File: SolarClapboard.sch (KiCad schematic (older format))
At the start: 52 parts, among them J1 TEST_1P, J2 TEST_1P, U1 MCP73871, U2 MPL3115A2, U3 HIH6130-I2C, U4 LT3011, U5 Teensy3.2

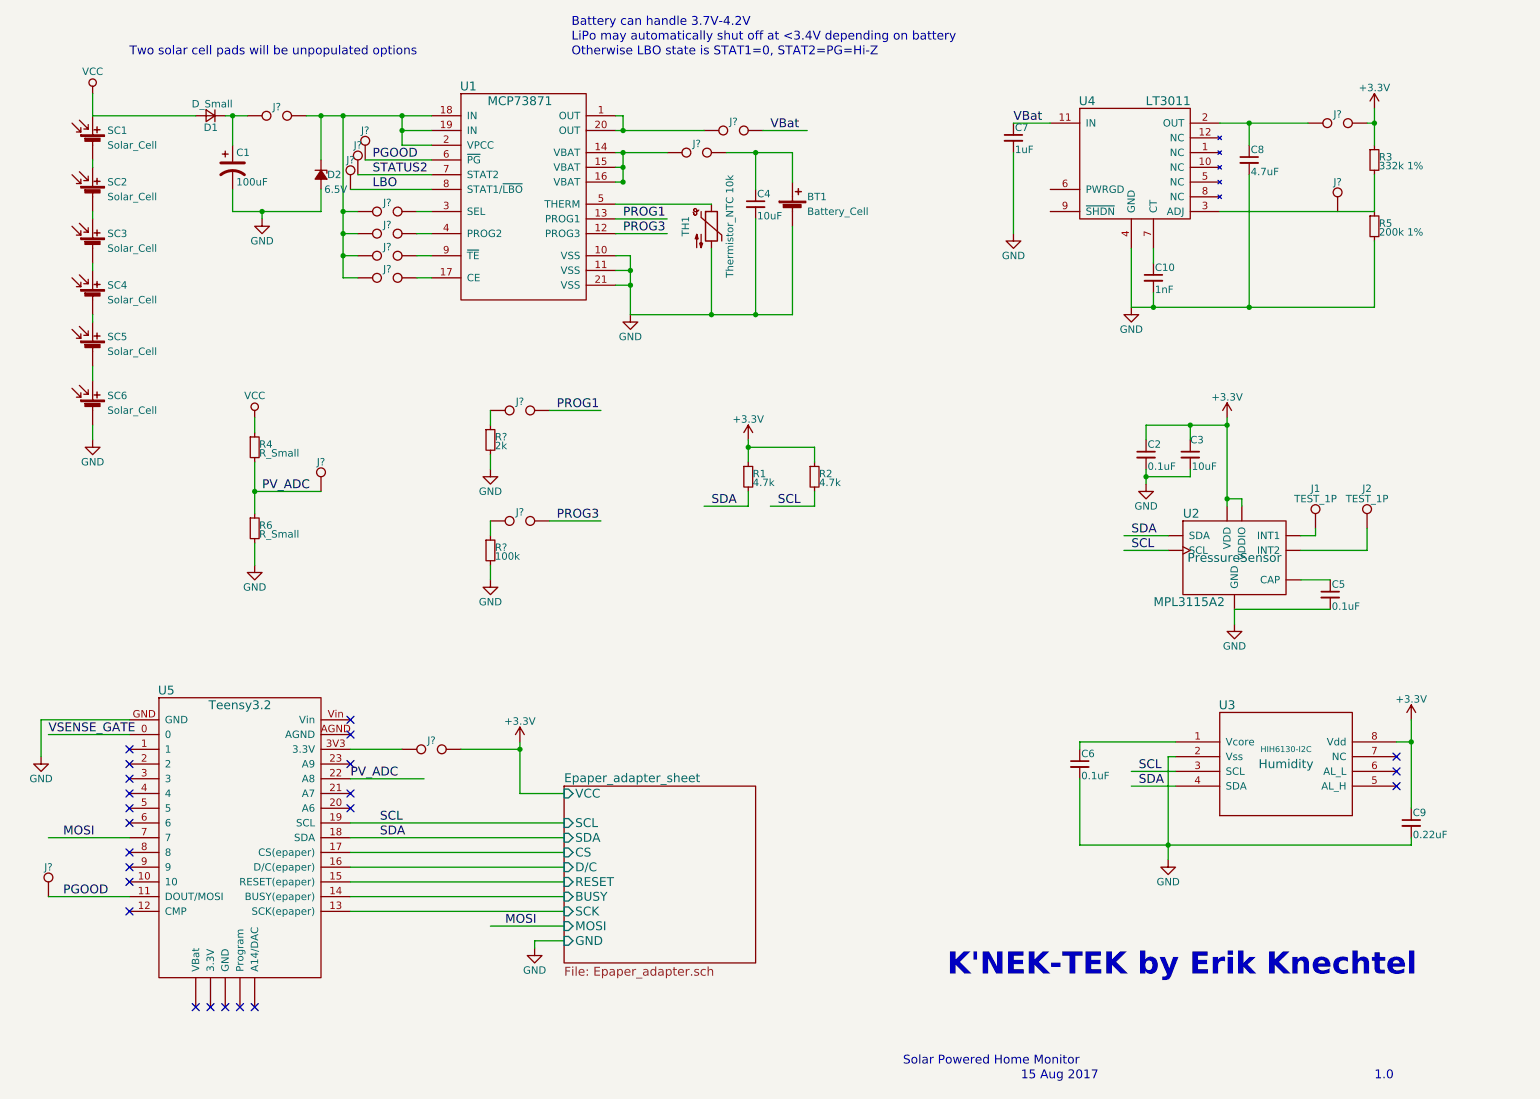
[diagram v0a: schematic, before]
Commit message: Add files via upload
Trying to figure out whether to hook up the PGOOD and PWRGOOD and SHDN and so on.
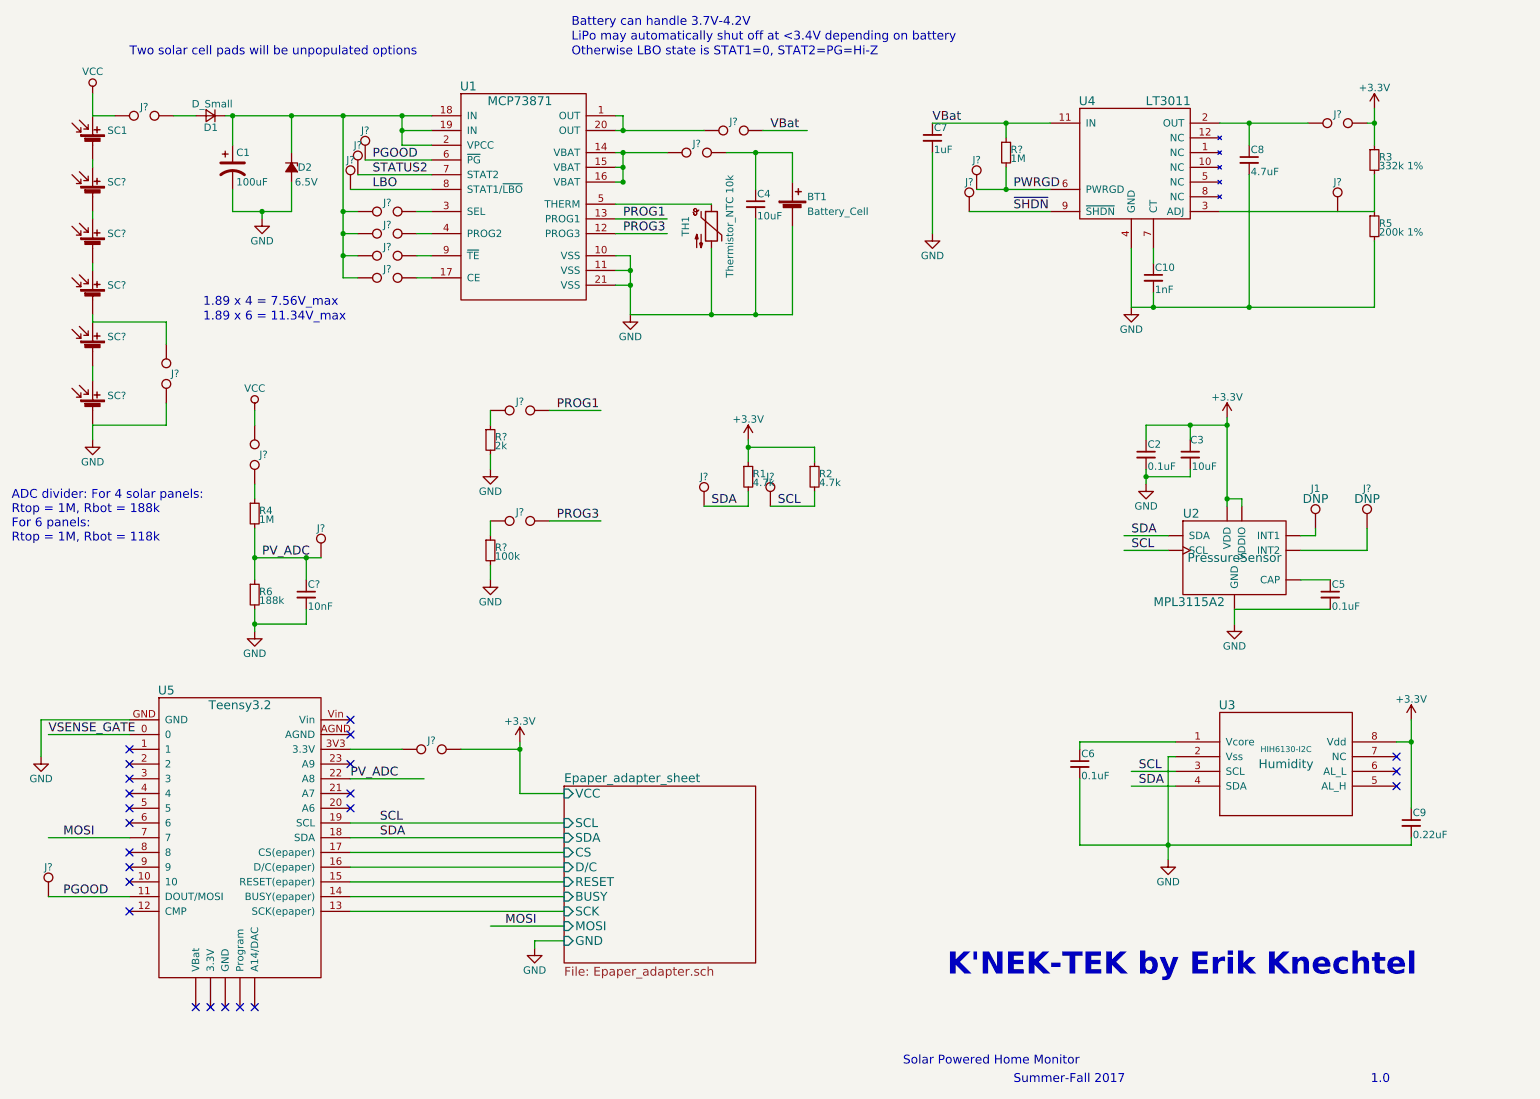
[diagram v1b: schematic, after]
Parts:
- removed J2: TEST_1P, symbol TEST_1P
- removed SC2, SC3, SC4, SC5, SC6: Solar_Cell, symbol Solar_Cell
- added C?: 10nF, symbol C_Small
- added J? (x2): TEST_2P, symbol TEST_2P
- added J? (x5): TEST_1P, symbol TEST_1P
- added R?: 1M, symbol R_Small
- added SC? (x5): Solar_Cell, symbol Solar_Cell
- J1: DNP (none) -> DNP
- R4: value R_Small -> 1M
- R6: value R_Small -> 188k
- SC1: MFG_PN (none) -> KXOB22-04X3F; Max_Current (none) -> 15mA; Max_Voltage (none) -> 1.89V; PMPP Current 18mA -> (none); PMPP Voltage 6.06V -> (none)
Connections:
- net labels added: PWRGD, ~SHDN
- wire segments 133 -> 145
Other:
- note added: "1.89 x 4 = 7.56V_max"
- note added: "1.89 x 6 = 11.34V_max"
- note added: "ADC divider: For 4 solar panels:\nRtop = 1M, Rbot = 188k\nFor 6 panels:\nRtop = 1M, Rbot = 118k\n"
- note added: "Summer-Fall 2017"
- note removed: "15 Aug 2017"
- moved on the sheet: C7, D2, J?, R4, R6

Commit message: Add files via upload
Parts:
- BT1: footprint (none) -> Connectors_JST:JST_PH_S2B-PH-SM4-TB_02x2.00mm_Angled
- J23: renamed from J?; footprint (none) -> Wire_Pads:SolderWirePad_single_1-2mmDrill
- U4: renamed from U3; footprint MODULE -> (none)
- gave numbers to parts that had none: 32
- renumbered C7 to C1, C6 to C10, C9 to C11, C8 to C2, C1 to C3, C10 to C5, C2 to C6, C3 to C7, C5 to C9, J1 to J21, R3 to R2, R5 to R3, R1 to R5, R2 to R6, R4 to R7, R6 to R9, U4 to U2, U2 to U3
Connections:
- net labels removed: VSENSE_GATE
- no-connect marks 23 -> 24
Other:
- moved on the sheet: J11

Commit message: Add files via upload
Working on the BOM and footprints.
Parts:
- C1, C10, C11, C2, C5, C6, C8, C9: footprint (none) -> Capacitors_SMD:C_1206_HandSoldering
- C3, C4: footprint (none) -> Capacitors_THT:CP_Radial_D5.0mm_P2.00mm
- J1, J12, J13, J14, J15, J16, J17, J2, J20, J24, J3, J4, J9: footprint (none) -> Measurement_Points:Test_Point_2Pads
- TP1: renamed from J7; footprint (none) -> Wire_Pads:SolderWirePad_single_1-2mmDrill
- TP10: renamed from J22; footprint (none) -> Wire_Pads:SolderWirePad_single_1-2mmDrill
- TP2: renamed from J6; footprint (none) -> Wire_Pads:SolderWirePad_single_1-2mmDrill
- TP3: renamed from J5; footprint (none) -> Wire_Pads:SolderWirePad_single_1-2mmDrill
- TP4: renamed from J25; footprint (none) -> Wire_Pads:SolderWirePad_single_1-2mmDrill
- TP6: renamed from J18; footprint (none) -> Wire_Pads:SolderWirePad_single_1-2mmDrill
- TP7: renamed from J19; footprint (none) -> Wire_Pads:SolderWirePad_single_1-2mmDrill
- TP8: renamed from J21; footprint (none) -> Wire_Pads:SolderWirePad_single_1-2mmDrill
- TP9: renamed from J11; footprint (none) -> Wire_Pads:SolderWirePad_single_1-2mmDrill
- U1: footprint (none) -> Housings_DFN_QFN:QFN-20-1EP_4x4mm_Pitch0.5mm; symbol MCP73871 -> MCP73871-RESCUE-SolarClapboard
- U2: footprint (none) -> Housings_SSOP:MSOP-12_3x4mm_Pitch0.65mm
- U3: footprint (none) -> CustomFootprints:LGA-8_3x5mm_Pitch1.25mm_handsolder
- U4: footprint (none) -> Housings_SOIC:SO-8_5.3x6.2mm_Pitch1.27mm
- renumbered J10 to TP30, J8 to TP31, J23 to TP5

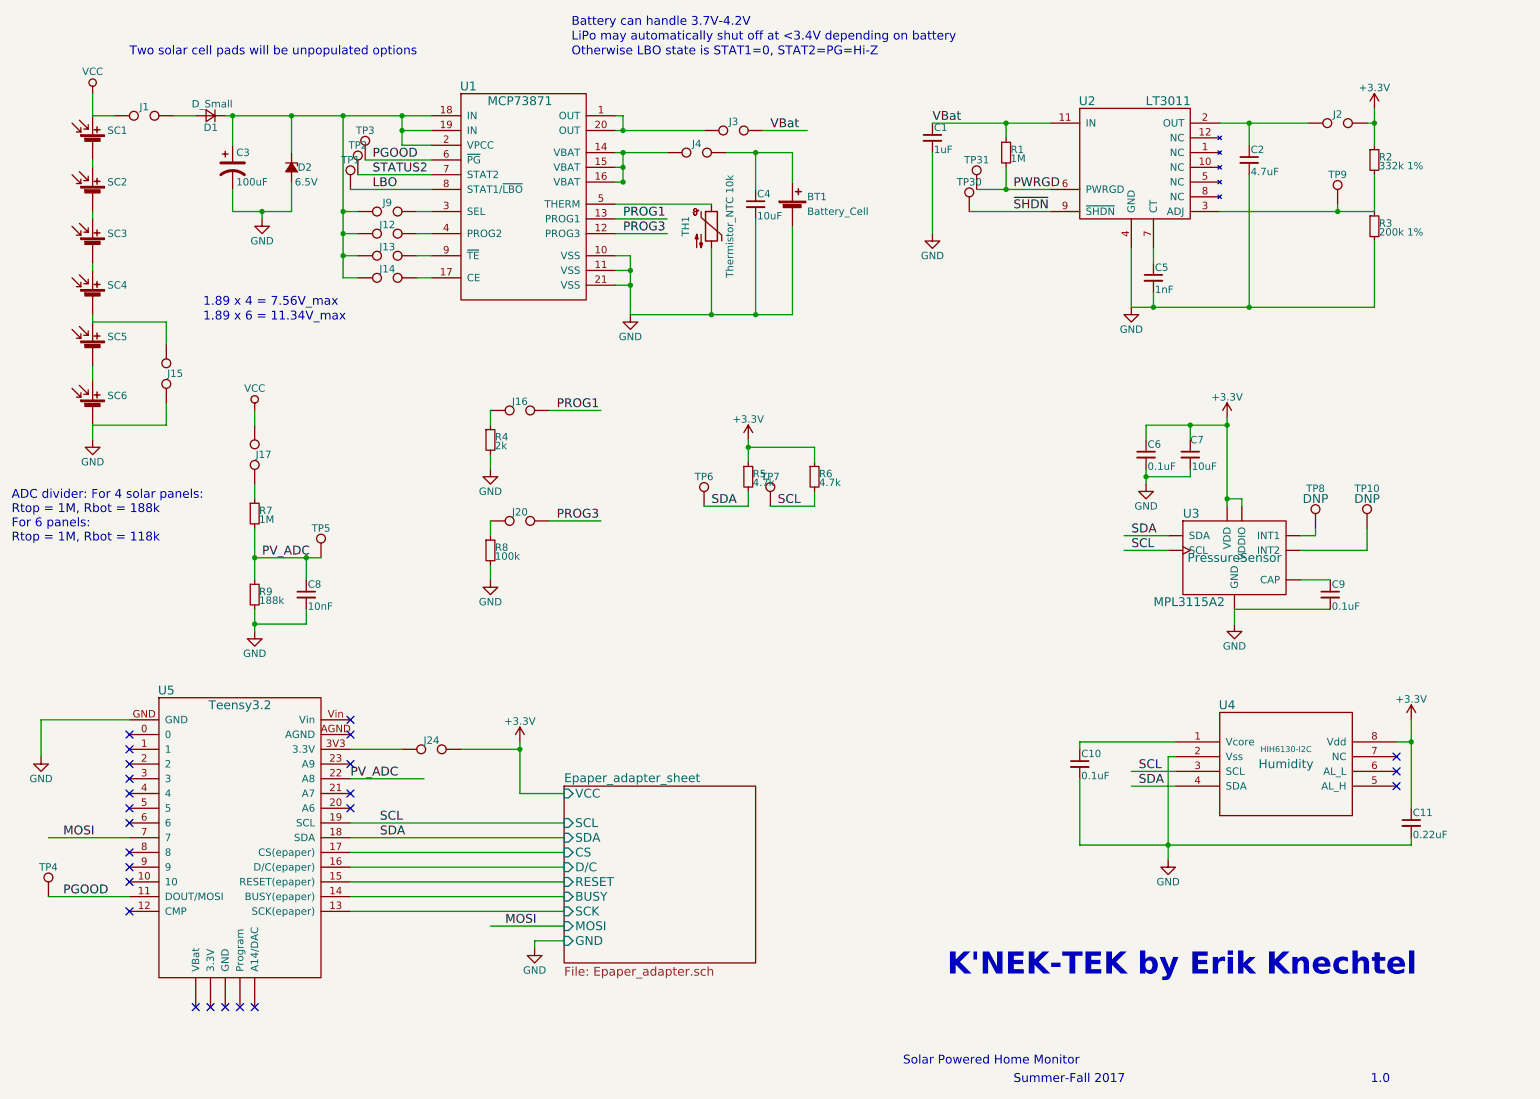
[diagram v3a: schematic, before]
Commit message: Add files via upload
Ready to do layout. All footprints correct, no board size chosen yet. Made outline for 6cm x 3.5cm e-paper.
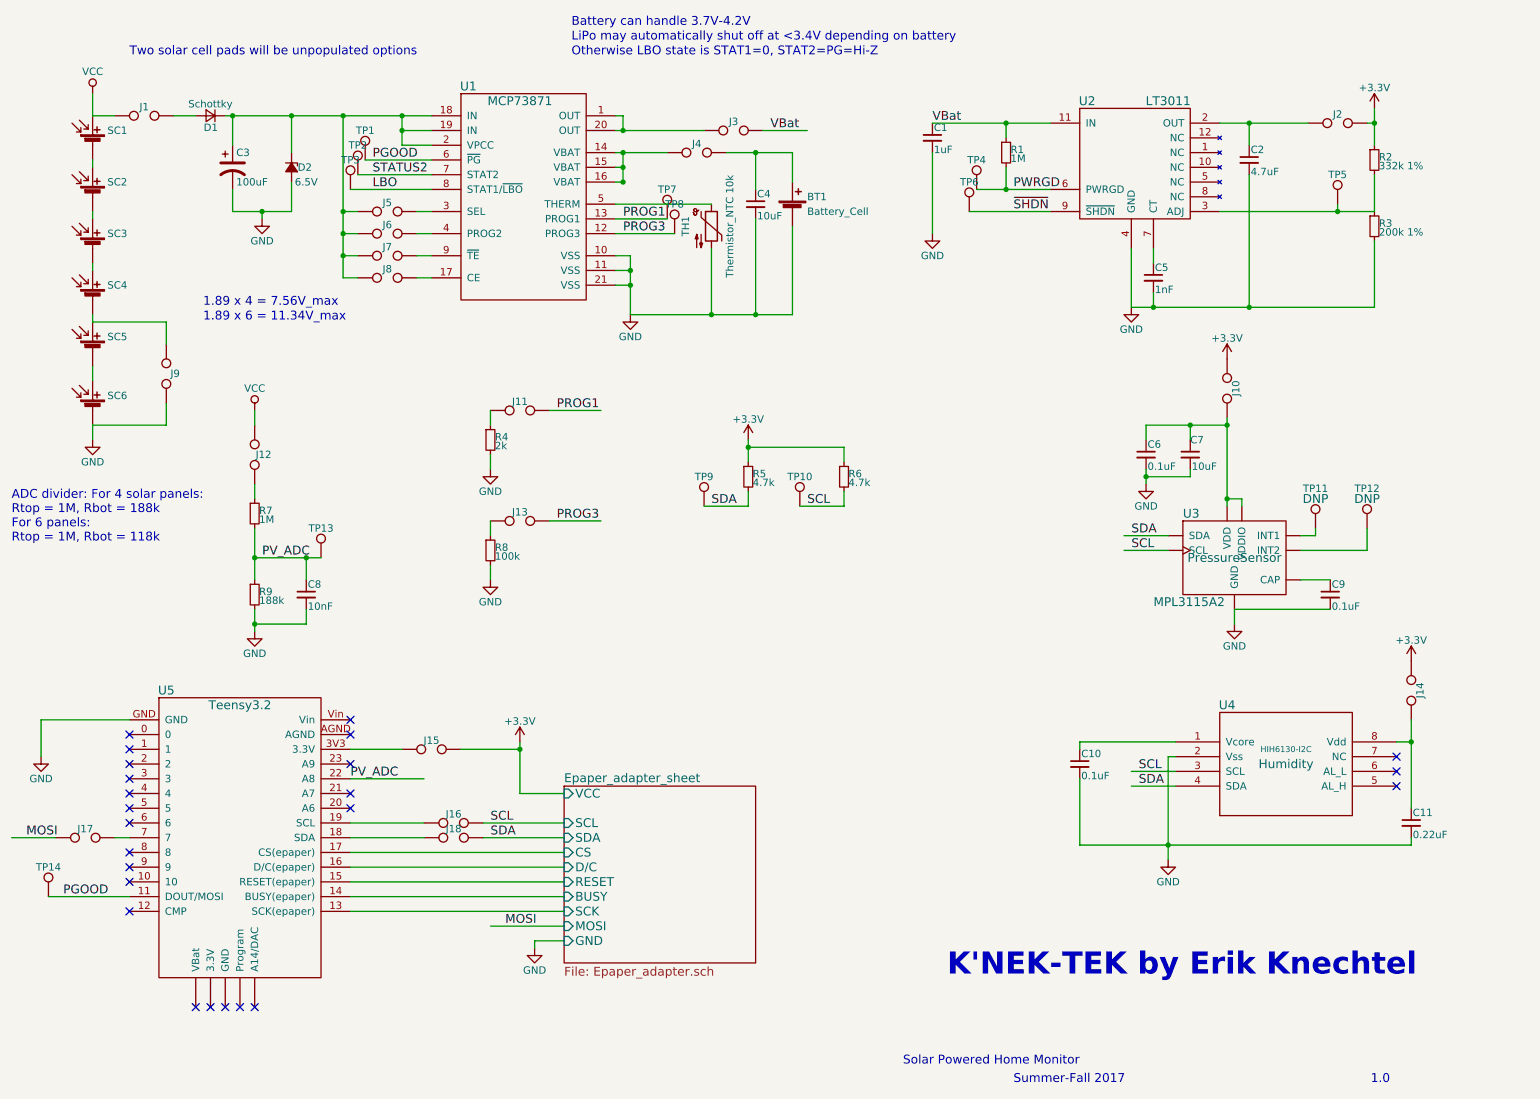
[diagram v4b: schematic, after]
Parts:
- added J10, J14, J16, J17, J18: TEST_2P, Measurement_Points:Test_Point_2Pads, symbol TEST_2P
- added TP7, TP8: TEST_1P, CustomFootprints:TestPointHole, symbol TEST_1P
- C7: footprint (none) -> Capacitors_THT:CP_Radial_D5.0mm_P2.00mm
- D1: value D_Small -> Schottky; footprint (none) -> Diodes_SMD:D_SOD-323_HandSoldering; MFG_PN (none) -> CUS08F30,H3F
- D2: footprint (none) -> Diodes_SMD:D_SOD-323_HandSoldering; MFG_PN (none) -> DDZ6V8ASF-7
- R1, R2, R3, R4, R5, R6, R7, R8, R9: footprint (none) -> Resistors_SMD:R_1206_HandSoldering
- SC1, SC2, SC3, SC4, SC5, SC6: footprint (none) -> CustomFootprints:MONO_SOLAR_CELL_22MMx7MM_KXOB22-04X3F
- TH1: footprint (none) -> Resistors_THT:R_Axial_DIN0204_L3.6mm_D1.6mm_P2.54mm_Vertical
- TP1: renamed from TP3; footprint Wire_Pads:SolderWirePad_single_1-2mmDrill -> CustomFootprints:TestPointHole
- TP10: renamed from TP7; footprint Wire_Pads:SolderWirePad_single_1-2mmDrill -> CustomFootprints:TestPointHole
- TP11: renamed from TP8; footprint Wire_Pads:SolderWirePad_single_1-2mmDrill -> CustomFootprints:TestPointHole
- TP12: renamed from TP10; footprint Wire_Pads:SolderWirePad_single_1-2mmDrill -> CustomFootprints:TestPointHole
- TP13: renamed from TP5; footprint Wire_Pads:SolderWirePad_single_1-2mmDrill -> CustomFootprints:TestPointHole
- TP14: renamed from TP4; footprint Wire_Pads:SolderWirePad_single_1-2mmDrill -> CustomFootprints:TestPointHole
- TP2: footprint Wire_Pads:SolderWirePad_single_1-2mmDrill -> CustomFootprints:TestPointHole
- TP3: renamed from TP1; footprint Wire_Pads:SolderWirePad_single_1-2mmDrill -> CustomFootprints:TestPointHole
- TP4: renamed from TP31; footprint (none) -> CustomFootprints:TestPointHole
- TP5: renamed from TP9; footprint Wire_Pads:SolderWirePad_single_1-2mmDrill -> CustomFootprints:TestPointHole
- TP6: renamed from TP30; footprint (none) -> CustomFootprints:TestPointHole
- TP9: renamed from TP6; footprint Wire_Pads:SolderWirePad_single_1-2mmDrill -> CustomFootprints:TestPointHole
- U5: footprint (none) -> CustomFootprints:Teensy_Header_Straight_2x14_Pitch2.54mm
- renumbered J16 to J11, J17 to J12, J20 to J13, J24 to J15, J9 to J5, J12 to J6, J13 to J7, J14 to J8, J15 to J9
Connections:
- wire segments 145 -> 148
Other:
- moved on the sheet: R6, TP10

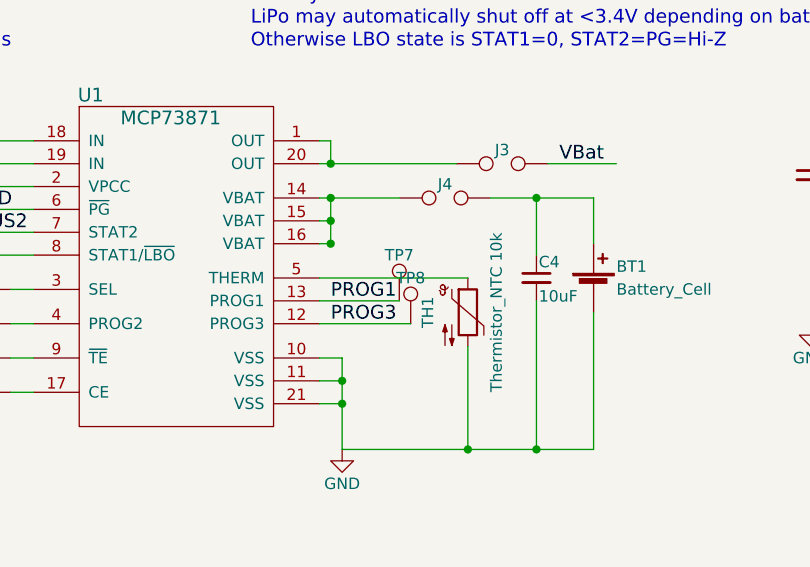
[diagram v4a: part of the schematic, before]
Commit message: Add files via upload
Ready for layout. Fixed test point hole size.
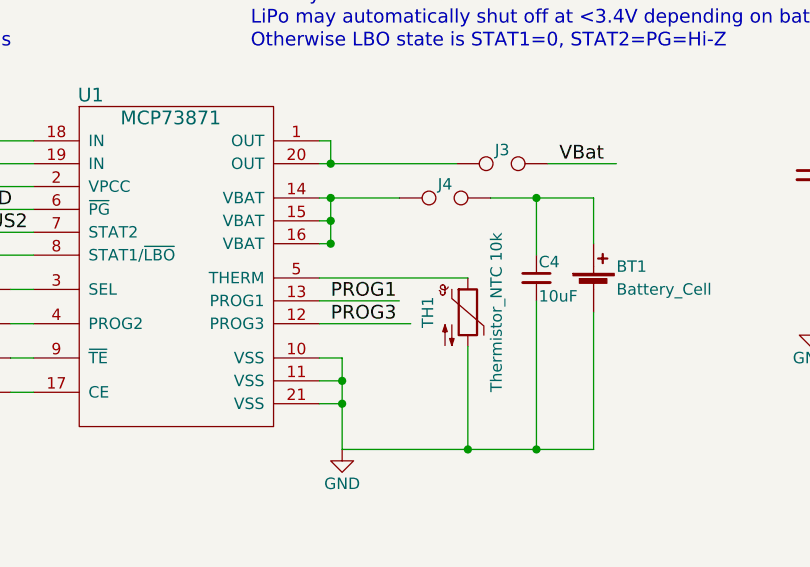
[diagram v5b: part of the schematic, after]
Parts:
- removed TP7, TP8: TEST_1P, CustomFootprints:TestPointHole, symbol TEST_1P
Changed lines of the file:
@@
 Wire Wire Line
 	950  6200 650  6200
-$Comp
-L TEST_1P TP7
-U 1 1 59FBF0E8
-P 5100 2000
-F 0 "TP7" H 5100 2200 50  0000 C CNN
-F 1 "TEST_1P" H 5100 2200 50  0001 C CNN
-F 2 "CustomFootprints:TestPointHole" H 5300 2000 50  0001 C CNN
-F 3 "" H 5300 2000 50  0001 C CNN
-	1    5100 2000
-	1    0    0    -1
-$EndComp
-$Comp
-L TEST_1P TP8
-U 1 1 59FBF24E
-P 5150 2100
-F 0 "TP8" H 5150 2300 50  0000 C CNN
-F 1 "TEST_1P" H 5150 2300 50  0001 C CNN
-F 2 "CustomFootprints:TestPointHole" H 5350 2100 50  0001 C CNN
-F 3 "" H 5350 2100 50  0001 C CNN
-	1    5150 2100
-	1    0    0    -1
-$EndComp
 Wire Wire Line
 	6300 3550 6300 3650
